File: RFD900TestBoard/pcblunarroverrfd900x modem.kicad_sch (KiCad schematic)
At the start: 8 parts, among them J1 Barrel_Jack, J2 Conn_02x08_Counter_Clockwise, U1 ESP32-DEVKIT-V1, U2 GPS-15136

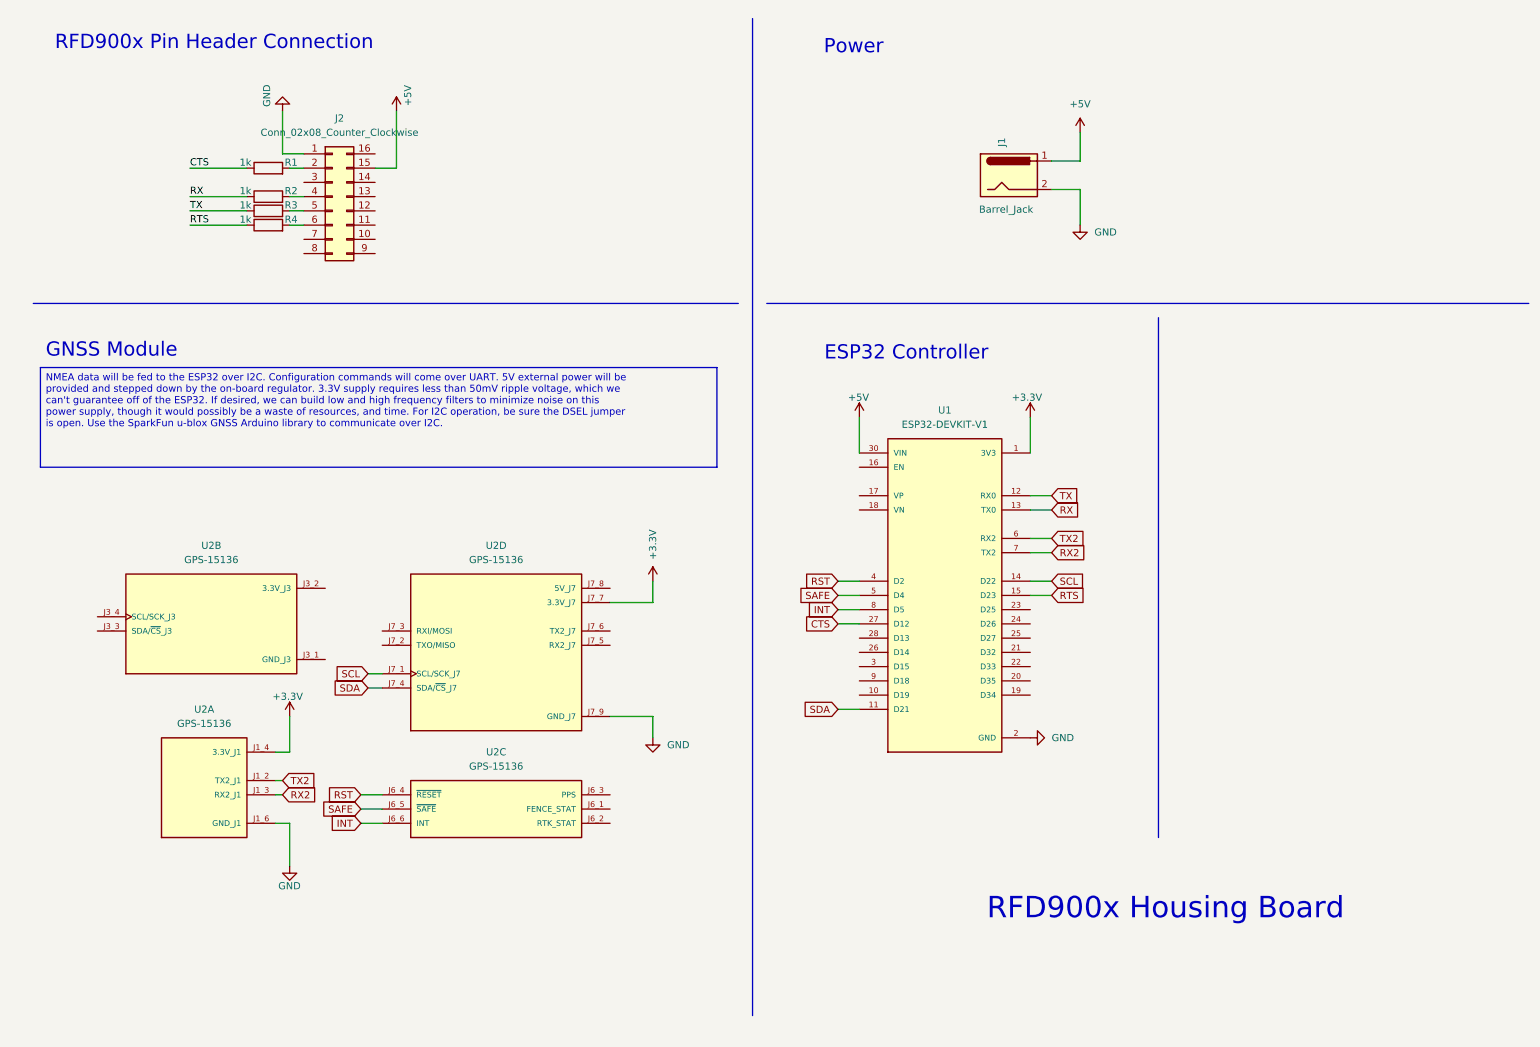
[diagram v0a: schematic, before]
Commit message: added jumpers to RFD900x Housing Board
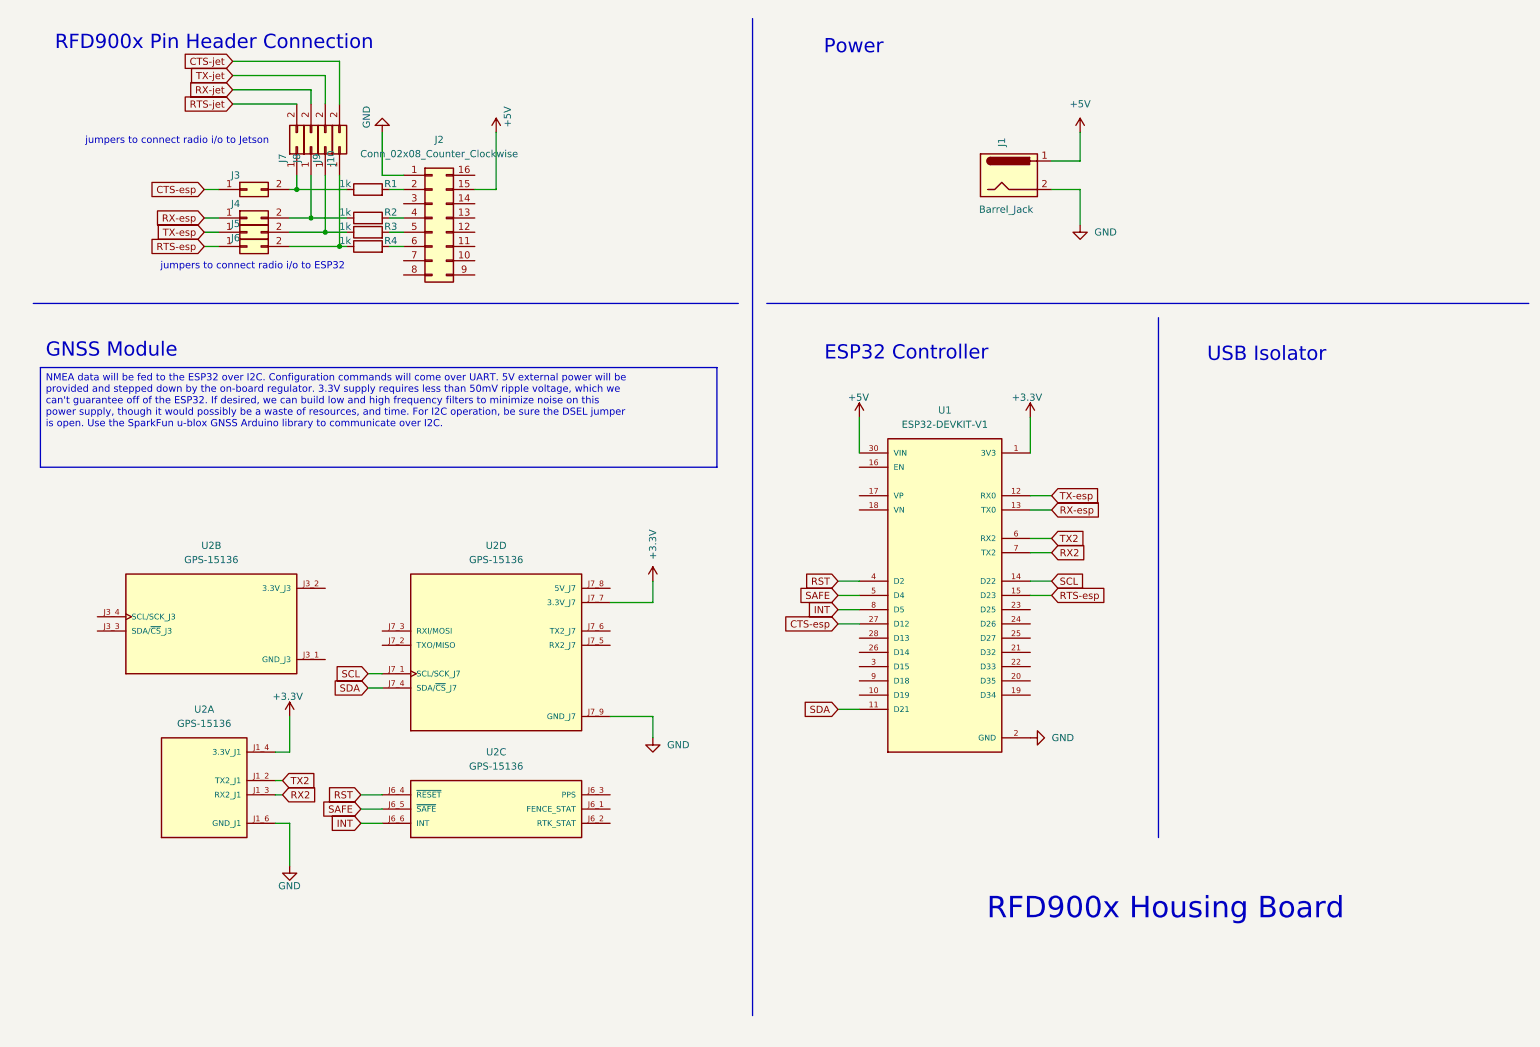
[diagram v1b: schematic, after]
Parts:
- added J10, J3, J4, J5, J6, J7, J8, J9: Conn_02x01, Connector_PinHeader_2.54mm:PinHeader_2x01_P2.54mm_Vertical, symbol Connector_Generic:Conn_02x01
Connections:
- net CTS: no longer names the net of R1.1
- net CTS: now also J3.2 (Pin_2), J7.1 (Pin_1); no longer U1.27 (D12)
- net RTS: no longer names the net of R4.1
- net RTS: now also J10.1 (Pin_1), J6.2 (Pin_2); no longer U1.15 (D23)
- net RX: no longer names the net of R2.1
- net RX: now also J4.2 (Pin_2), J8.1 (Pin_1); no longer U1.13 (TX0)
- net TX: no longer names the net of R3.1
- net TX: now also J5.2 (Pin_2), J9.1 (Pin_1); no longer U1.12 (RX0)
- new net CTS-esp: J3.1 (Pin_1), U1.27 (D12)
- new net CTS-jet: J10.2 (Pin_2)
- new net RTS-esp: J6.1 (Pin_1), U1.15 (D23)
- new net RTS-jet: J7.2 (Pin_2)
- new net RX-esp: J4.1 (Pin_1), U1.13 (TX0)
- new net RX-jet: J8.2 (Pin_2)
- new net TX-esp: J5.1 (Pin_1), U1.12 (RX0)
- new net TX-jet: J9.2 (Pin_2)
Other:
- note added: "USB Isolator"
- note added: "jumpers to connect radio i/o to ESP32"
- note added: "jumpers to connect radio i/o to Jetson"
- moved on the sheet: J2, R1, R2, R3, R4

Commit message: almost done with RFD900x Test Board
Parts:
- added D1: LED, symbol Device:LED
- added J11, J12, J14, J15, J16, J17: Conn_02x01, Connector_PinHeader_2.54mm:PinHeader_2x01_P2.54mm_Vertical, symbol Connector_Generic:Conn_02x01
- added J13: Conn_01x09, symbol Connector_Generic:Conn_01x09
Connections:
- net CTS-jet: now also J13.1 (Pin_1)
- net GND: now also D1.1 (K)
- net RTS-jet: now also J13.4 (Pin_4)
- net RX-jet: now also J13.3 (Pin_3)
- net RX2: now also J15.1 (Pin_1); no longer U2.J1_3 (RX2_J1)
- net SCL: no longer U2.J7_1 (SCL/SCK_J7)
- net SDA: no longer U2.J7_4 (SDA/~{CS}_J7)
- net TX-jet: now also J13.2 (Pin_2)
- net TX2: now also J14.1 (Pin_1); no longer U2.J1_2 (TX2_J1)
- net at U2.J7_5 (RX2_J7): now also J15.2 (Pin_2), J17.2 (Pin_2)
- net at U2.J7_6 (TX2_J7): now also J14.2 (Pin_2), J16.2 (Pin_2)
- net RTK-jet: now reaches U2.J6_2 (RTK_STAT)
- net RTK-jet: now also D1.2 (A), J13.7 (Pin_7)
- net SAFE: no longer names the net of U1.5 (D4)
- net SAFE: no longer U2.J6_5 (~{SAFE})
- new net: J12.1 (Pin_1), U2.J7_1 (SCL/SCK_J7)
- new net: J11.1 (Pin_1), U2.J7_4 (SDA/~{CS}_J7)
- new net RX2-jet: J13.8 (Pin_8), J16.1 (Pin_1)
- new net SCL-jet: J12.2 (Pin_2), J13.6 (Pin_6)
- new net SDA-jet: J11.2 (Pin_2), J13.5 (Pin_5)
- new net TX2-jet: J13.9 (Pin_9), J17.1 (Pin_1)
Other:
- note added: "For RTCM correction"
- note added: "JETSON/Host PC"
- note added: "NMEA Data"
- note removed: "USB Isolator"
- moved on the sheet: U2A, U2B, U2D

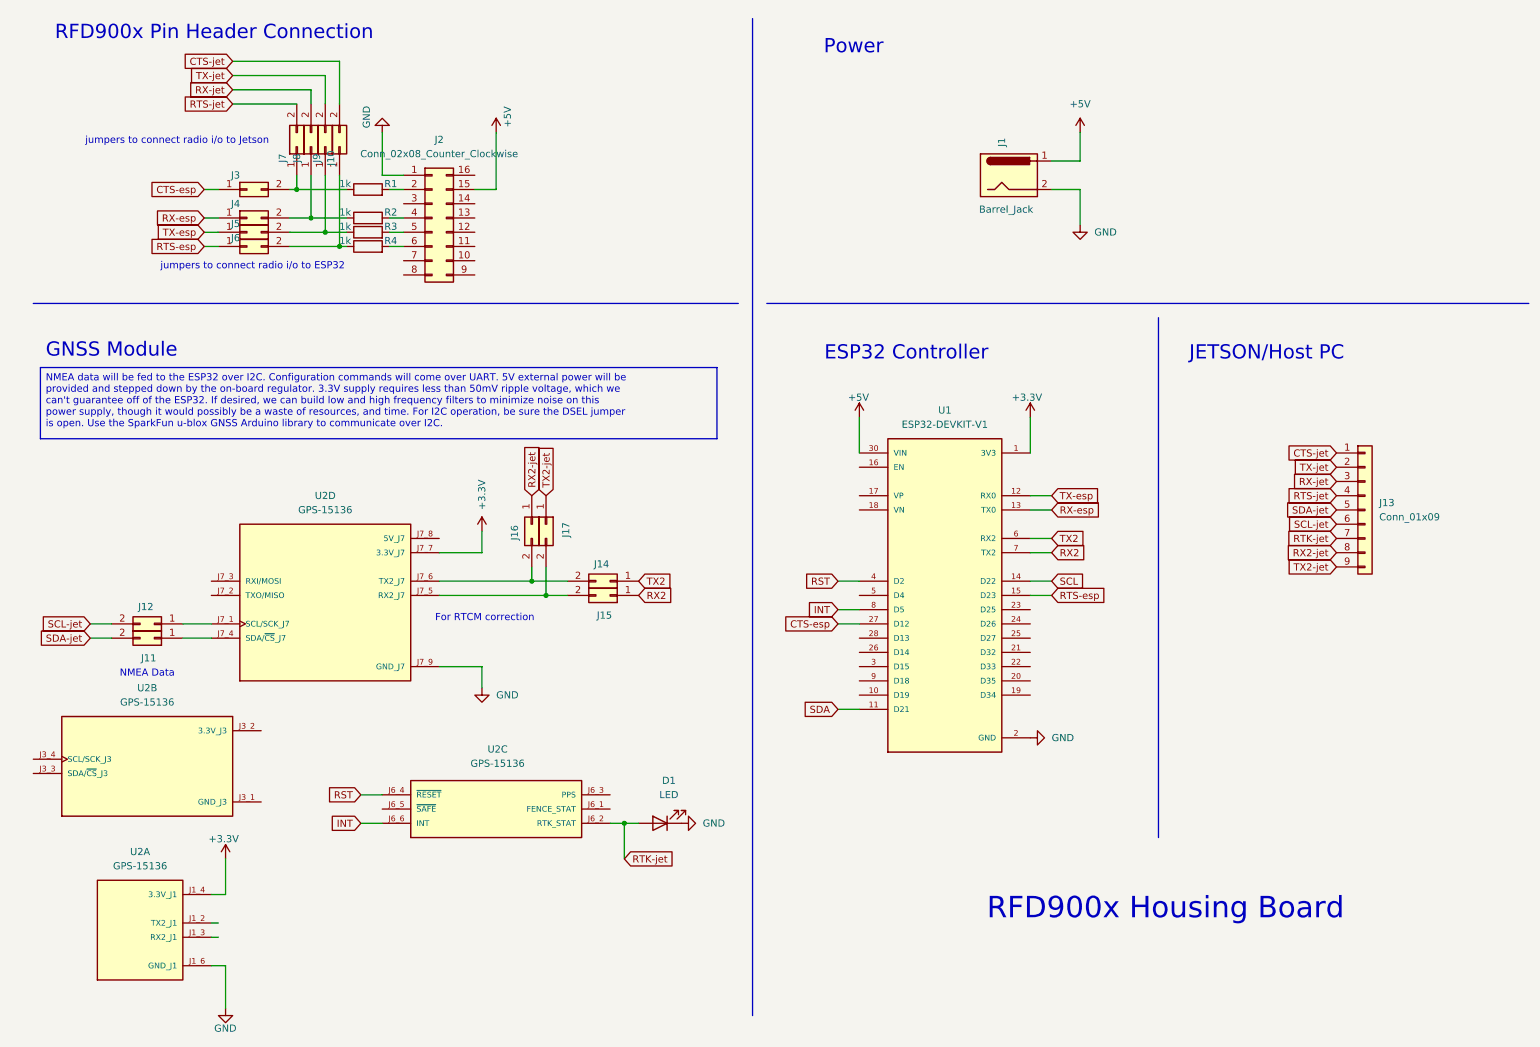
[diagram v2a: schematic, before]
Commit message: made final touches to schematic
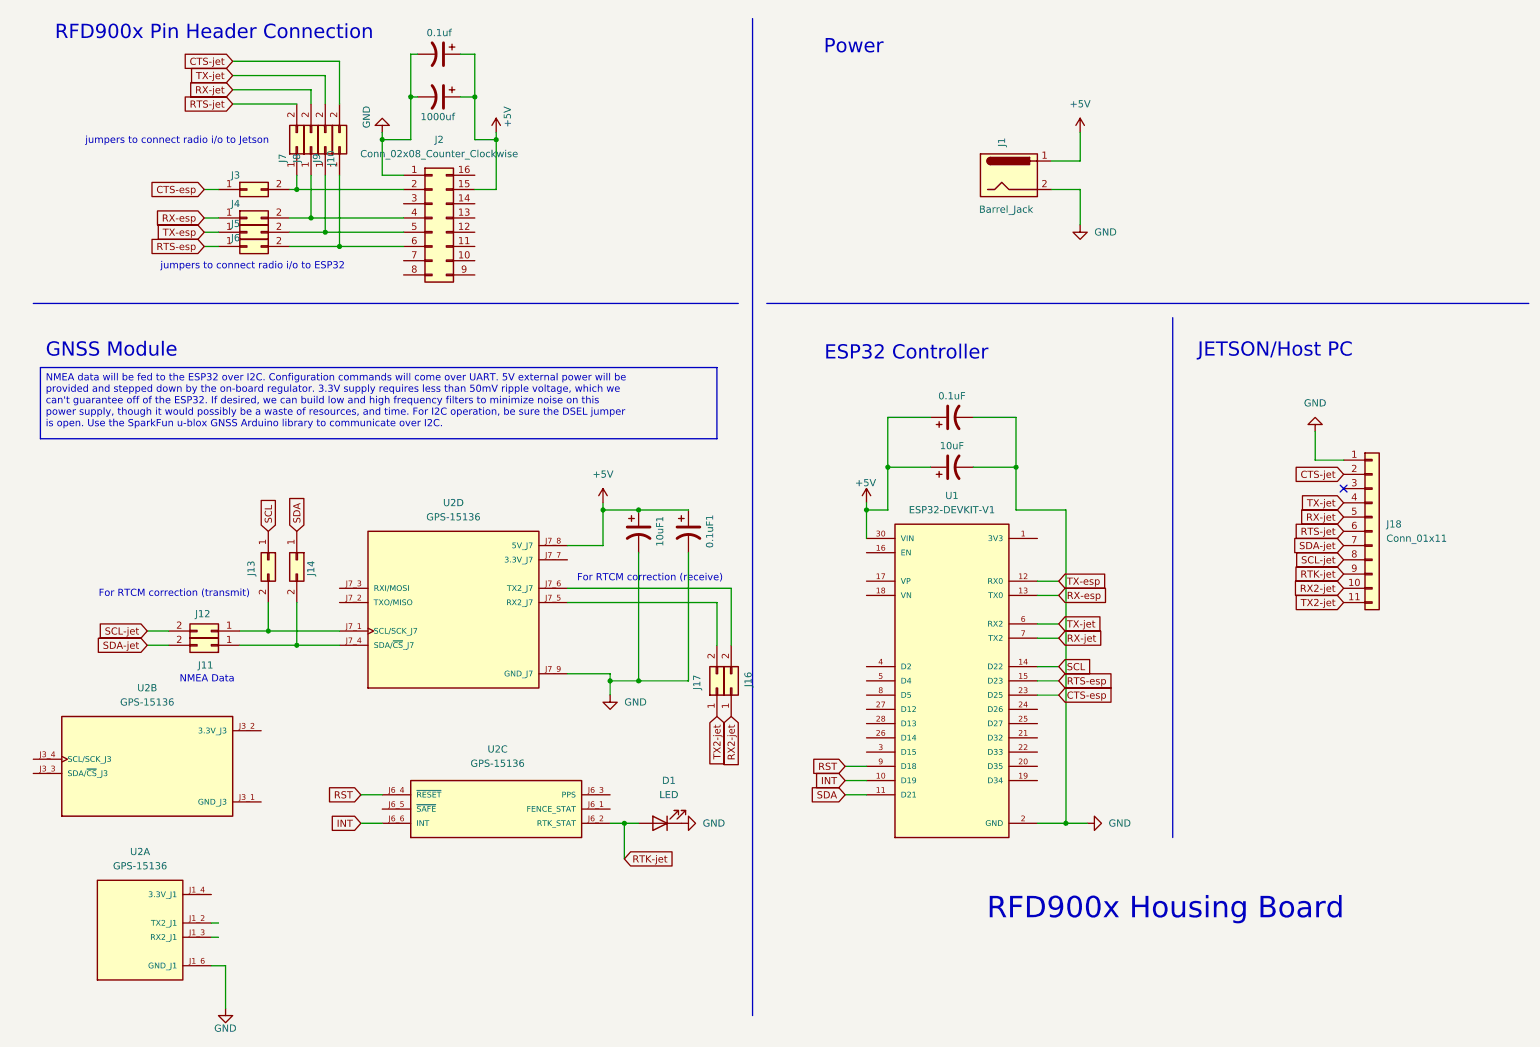
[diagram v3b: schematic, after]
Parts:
- removed J13: Conn_01x09, symbol Connector_Generic:Conn_01x09
- removed J15: Conn_02x01, Connector_PinHeader_2.54mm:PinHeader_2x01_P2.54mm_Vertical, symbol Connector_Generic:Conn_02x01
- removed R1, R2, R3, R4: 1k, \, symbol Device:R
- added 0.1uF, 0.1uF1, 0.1uf, 1000uf, 10uF, 10uF1: C_Polarized_US, symbol Device:C_Polarized_US
- added J13: Conn_02x01, Connector_PinHeader_2.54mm:PinHeader_2x01_P2.54mm_Vertical, symbol Connector_Generic:Conn_02x01
- added J18: Conn_01x11, symbol Connector_Generic:Conn_01x11
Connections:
- net RX2 is gone; now on net RX-jet: U1.7 (TX2)
- net +5V: now also U2.J7_8 (5V_J7), 0.1uF.1, 0.1uF1.1, 0.1uf.1, 1000uf.1, 10uF.1, 10uF1.1
- net CTS-esp: now also U1.23 (D25); no longer U1.27 (D12)
- net CTS-jet: now also J18.2 (Pin_2)
- net GND: now also 0.1uF.2, 0.1uF1.2, 0.1uf.2, 1000uf.2, 10uF.2, 10uF1.2, J18.1 (Pin_1)
- net INT: now also U1.10 (D19); no longer U1.8 (D5)
- net RST: now also U1.9 (D18); no longer U1.4 (D2)
- net RTK-jet: now also J18.9 (Pin_9)
- net RTS-jet: now also J18.6 (Pin_6)
- net RX-jet: now also J18.5 (Pin_5)
- net RX2-jet: now also J18.10 (Pin_10)
- net SCL: now also J13.1 (Pin_1)
- net SCL-jet: now also J18.8 (Pin_8)
- net SDA: now also J14.1 (Pin_1)
- net SDA-jet: now also J18.7 (Pin_7)
- net TX-jet: now also U1.6 (RX2), J18.4 (Pin_4)
- net TX2-jet: now also J18.11 (Pin_11)
- net at J5.2 (Pin_2), J9.1 (Pin_1): now also J2.5 (Pin_5)
- net at J4.2 (Pin_2), J8.1 (Pin_1): now also J2.4 (Pin_4)
- net at J3.2 (Pin_2), J7.1 (Pin_1): now also J2.2 (Pin_2)
- net at J16.2 (Pin_2), U2.J7_6 (TX2_J7): no longer J14.2 (Pin_2)
- net at J12.1 (Pin_1), U2.J7_1 (SCL/SCK_J7): now also J13.2 (Pin_2)
- net at J11.1 (Pin_1), U2.J7_4 (SDA/~{CS}_J7): now also J14.2 (Pin_2)
- net at J10.1 (Pin_1), J6.2 (Pin_2): now also J2.6 (Pin_6)
- removed net +3.3V: U1.1 (3V3), U2.J1_4 (3.3V_J1), U2.J7_7 (3.3V_J7)
- removed net TX2: J14.1 (Pin_1), U1.6 (RX2)
- no-connect marks 0 -> 1
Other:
- note added: "For RTCM correction (receive)"
- note added: "For RTCM correction (transmit)"
- note removed: "For RTCM correction"
- moved on the sheet: J11, J12, J16, J17, U1, U2D

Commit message: edits
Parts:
- 0.1uF1, 10uF1: footprint (none) -> Capacitor_THT:CP_Radial_D5.0mm_P2.00mm
- 0.1uF3: renamed from 0.1uF; footprint (none) -> Capacitor_THT:CP_Radial_D5.0mm_P2.00mm
- 0.1uf2: renamed from 0.1uf; footprint (none) -> Capacitor_THT:CP_Radial_D5.0mm_P2.00mm
- 1000uf1: renamed from 1000uf; footprint (none) -> Capacitor_THT:CP_Radial_D5.0mm_P2.00mm
- 10uF2: renamed from 10uF; footprint (none) -> Capacitor_THT:CP_Radial_D5.0mm_P2.00mm
- D1: footprint (none) -> LED_THT:LED_D3.0mm
- J18: footprint (none) -> Connector_PinHeader_2.54mm:PinHeader_1x11_P2.54mm_Vertical
- J2: footprint Connector_DIN:DIN41612_B2_2x8_Male_Horizontal_THT -> Connector_PinHeader_2.54mm:PinHeader_2x08_P2.54mm_Vertical
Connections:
- net +5V: now also J2.4 (Pin_4); no longer J2.15 (Pin_15)
- net at J5.2 (Pin_2), J9.1 (Pin_1): now also J2.9 (Pin_9); no longer J2.5 (Pin_5)
- net at J3.2 (Pin_2), J7.1 (Pin_1): now also J2.3 (Pin_3); no longer J2.2 (Pin_2)
- net at J4.2 (Pin_2), J8.1 (Pin_1): now also J2.7 (Pin_7); no longer J2.4 (Pin_4)
- net at J2.11 (Pin_11): now also J10.1 (Pin_1), J6.2 (Pin_2)
- now unconnected: J2.6 (Pin_6)
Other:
- moved on the sheet: 0.1uf2, 1000uf1, J2
